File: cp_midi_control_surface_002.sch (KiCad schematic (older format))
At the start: 44 parts, among them J10 Conn_01x08_Female, J11 Conn_01x08_Female, J12 Conn_01x08_Female, J13 Conn_01x08_Female, J18 Conn_01x01_Male, J19 Conn_01x01_Male, J20 Conn_01x01_Male, J21 Conn_01x01_Male, J22 Conn_01x01_Male, J23 Conn_01x01_Male, P1 Digital, P2 Power, P3 Analogue, P4 Analogue, P5 PWM, P6 PWM, P7 Communication

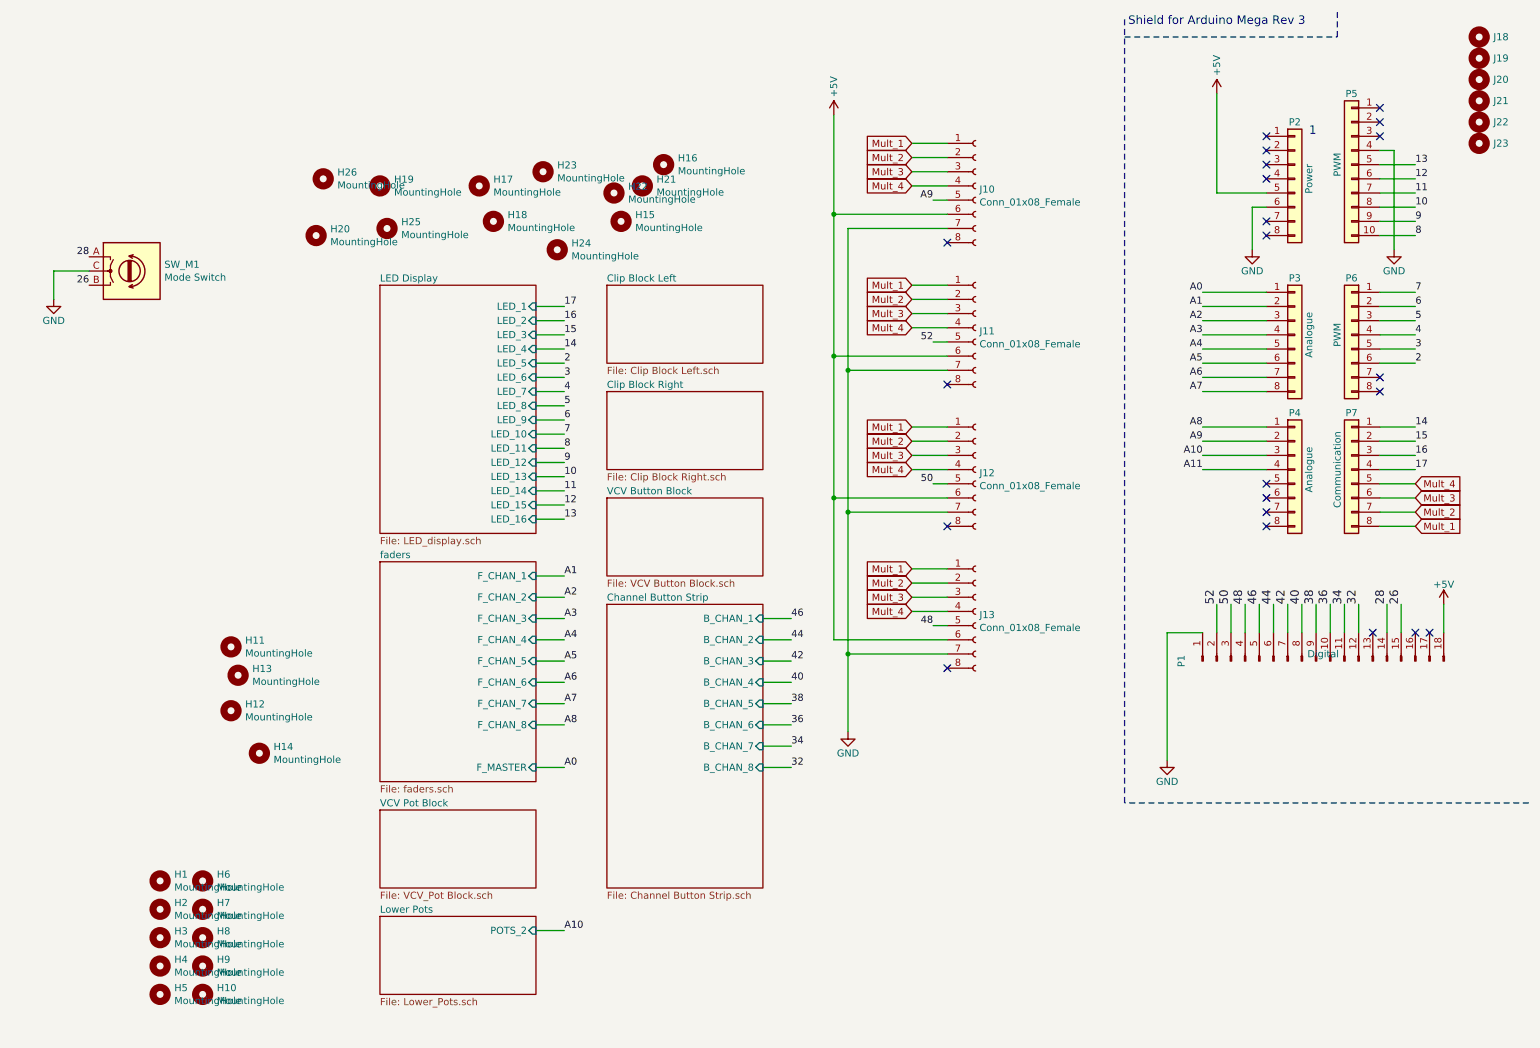
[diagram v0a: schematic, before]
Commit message: First of changes due to different software
Moving and analogue inputs, correcting for placement of multiplexer pads.
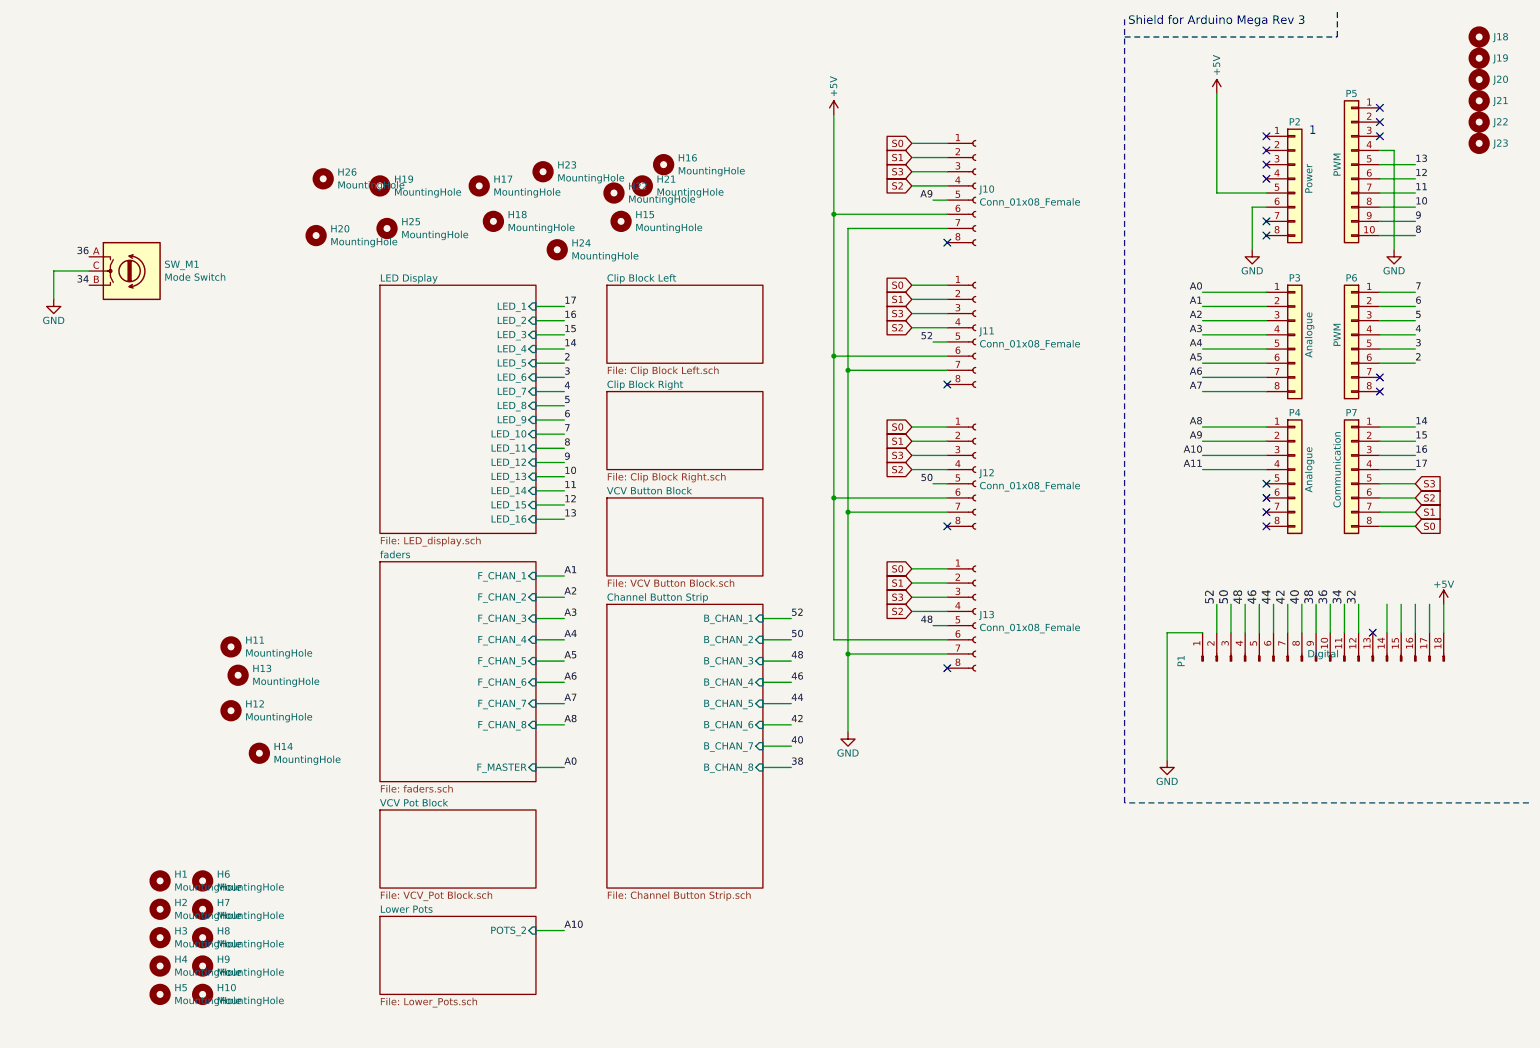
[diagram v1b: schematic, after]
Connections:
- net 34: now also SW_M1.B
- net 36: now also SW_M1.A
- net 26: no longer names the net of P1.15 (Pin_15)
- net 26: no longer SW_M1.B
- net 28: no longer names the net of P1.14 (Pin_14)
- net 28: no longer SW_M1.A
- net Mult_1 renamed S0
- net Mult_2 renamed S1
- net Mult_3 renamed S3
- net S3: now also P7.5 (Pin_5); no longer P7.6 (Pin_6)
- net Mult_4 renamed S2
- net S2: now also P7.6 (Pin_6); no longer P7.5 (Pin_5)
- no-connect marks 22 -> 20
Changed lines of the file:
@@
 Text Label 8900 3700 2    50   ~ 0
 A11
-Text Label 10300 4650 1    60   ~ 0
-26
-Text Label 10200 4650 1    60   ~ 0
-28
 Text Label 10000 4650 1    60   ~ 0
 32
@@
 $EndComp
 Text Label 1050 2200 2    50   ~ 0
-28
+36
 Text Label 1050 2400 2    50   ~ 0
-26
+34
 $Comp
 L power:GND #PWR07
@@
 A1
 Text GLabel 10400 4100 2    50   Input ~ 0
-Mult_1
+S0
 Text GLabel 10400 4000 2    50   Input ~ 0
-Mult_2
+S1
 Text GLabel 10400 3900 2    50   Input ~ 0
-Mult_3
+S2
 $Sheet
 S 3100 2400 1100 1750
@@
 	6000 5800 5800 5800
 Text Label 6000 4750 0    50   ~ 0
+52
+Text Label 6000 4900 0    50   ~ 0
+50
+Text Label 6000 5200 0    50   ~ 0
 46
-Text Label 6000 4900 0    50   ~ 0
+Text Label 6000 5050 0    50   ~ 0
+48
+Text Label 6000 5350 0    50   ~ 0
 44
-Text Label 6000 5200 0    50   ~ 0
+Text Label 6000 5500 0    50   ~ 0
+42
+Text Label 6000 5650 0    50   ~ 0
 40
-Text Label 6000 5050 0    50   ~ 0
-42
-Text Label 6000 5350 0    50   ~ 0
+Text Label 6000 5800 0    50   ~ 0
 38
-Text Label 6000 5500 0    50   ~ 0
-36
-Text Label 6000 5650 0    50   ~ 0
-34
-Text Label 6000 5800 0    50   ~ 0
-32
 Text GLabel 10400 3800 2    50   Input ~ 0
-Mult_4
+S3
 NoConn ~ 10150 3050
 NoConn ~ 10150 3150
@@
 NoConn ~ 10150 1250
 NoConn ~ 10150 1150
-NoConn ~ 10400 4850
-NoConn ~ 10500 4850
 Wire Wire Line
 	8650 4850 8650 5750
@@
 	1    0    0    -1
 $EndComp
-Text GLabel 6850 1400 0    50   Input ~ 0
-Mult_1
-Text GLabel 6850 1500 0    50   Input ~ 0
-Mult_2
-Text GLabel 6850 1600 0    50   Input ~ 0
-Mult_3
-Text GLabel 6850 1700 0    50   Input ~ 0
-Mult_4
+Text GLabel 6850 2400 0    50   Input ~ 0
+S0
+Text GLabel 6850 2500 0    50   Input ~ 0
+S1
+Text GLabel 6850 2700 0    50   Input ~ 0
+S2
+Text GLabel 6850 2600 0    50   Input ~ 0
+S3
 Wire Wire Line
 	6850 1700 7100 1700
@@
 	1    0    0    -1
 $EndComp
-Text GLabel 6850 3400 0    50   Input ~ 0
-Mult_1
-Text GLabel 6850 3500 0    50   Input ~ 0
-Mult_2
-Text GLabel 6850 3600 0    50   Input ~ 0
-Mult_3
-Text GLabel 6850 3700 0    50   Input ~ 0
-Mult_4
 Wire Wire Line
 	6850 3700 7100 3700
@@
 	1    0    0    -1
 $EndComp
-Text GLabel 6850 2400 0    50   Input ~ 0
-Mult_1
-Text GLabel 6850 2500 0    50   Input ~ 0
-Mult_2
-Text GLabel 6850 2600 0    50   Input ~ 0
-Mult_3
-Text GLabel 6850 2700 0    50   Input ~ 0
-Mult_4
 Wire Wire Line
 	6850 2700 7100 2700
@@
 	1    0    0    -1
 $EndComp
-Text GLabel 6850 4400 0    50   Input ~ 0
-Mult_1
-Text GLabel 6850 4500 0    50   Input ~ 0
-Mult_2
-Text GLabel 6850 4600 0    50   Input ~ 0
-Mult_3
-Text GLabel 6850 4700 0    50   Input ~ 0
-Mult_4
 Wire Wire Line
 	6850 4700 7100 4700
@@
 	1    0    0    -1
 $EndComp
+Text GLabel 6850 1400 0    50   Input ~ 0
+S0
+Text GLabel 6850 1500 0    50   Input ~ 0
+S1
+Text GLabel 6850 1700 0    50   Input ~ 0
+S2
+Text GLabel 6850 1600 0    50   Input ~ 0
+S3
+Text GLabel 6850 3400 0    50   Input ~ 0
+S0
+Text GLabel 6850 3500 0    50   Input ~ 0
+S1
+Text GLabel 6850 3700 0    50   Input ~ 0
+S2
+Text GLabel 6850 3600 0    50   Input ~ 0
+S3
+Text GLabel 6850 4400 0    50   Input ~ 0
+S0
+Text GLabel 6850 4500 0    50   Input ~ 0
+S1
+Text GLabel 6850 4700 0    50   Input ~ 0
+S2
+Text GLabel 6850 4600 0    50   Input ~ 0
+S3
+Wire Wire Line
+	10400 4650 10400 4850
+Wire Wire Line
+	10500 4650 10500 4850
 $EndSCHEMATC

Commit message: Sub boards completed
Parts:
- removed P4: Analogue, Socket_Arduino_Mega:Socket_Strip_Arduino_1x08, symbol Connector_Generic:Conn_01x08
- H1, H10, H11, H12, H13, H14, H15, H16, H17, H18, H19, H2, H20, H21, H22, H23, H24, H25, H26, H3, H4, H5, H6, H7, H8, H9: footprint cunabulapress-footprints:Mounting_Hole_3.2mm_M3 -> cunabulapress-footprints:Mounting_Hole_M3_with_Target
- P2, P3, P6: footprint Socket_Arduino_Mega:Socket_Strip_Arduino_1x08 -> Connector_PinHeader_2.54mm:PinHeader_1x08_P2.54mm_Vertical
- P5: footprint Socket_Arduino_Mega:Socket_Strip_Arduino_1x10 -> Connector_PinHeader_2.54mm:PinHeader_1x10_P2.54mm_Vertical
- P7: footprint Socket_Arduino_Mega:Socket_Strip_Arduino_1x08 -> Connector_PinHeader_2.54mm:PinHeader_1x04_P2.54mm_Vertical; symbol Connector_Generic:Conn_01x08 -> Connector_Generic:Conn_01x04
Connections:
- net A9 is gone; now on net A0: J10.5 (Pin_5)
- net A1: now also J11.5 (Pin_5)
- net A2: now also J12.5 (Pin_5)
- net A3: now also J13.5 (Pin_5)
- net S0: now also P1.17 (Pin_17); no longer P7.8 (Pin_8)
- net S1: now also P1.16 (Pin_16); no longer P7.7 (Pin_7)
- net S2: now also P1.14 (Pin_14); no longer P7.6 (Pin_6)
- net S3: now also P1.15 (Pin_15); no longer P7.5 (Pin_5)
- net 32 renamed 33
- net 34 renamed 35
- net 36 renamed 37
- net 38 renamed 39
- net 40 renamed 41
- net 42 renamed 43
- net 44 renamed 45
- net 46 renamed 47
- net 48 renamed 49
- net 49: no longer J13.5 (Pin_5)
- net 50 renamed 51
- net 51: no longer J12.5 (Pin_5)
- net 52 renamed 53
- net 53: no longer J11.5 (Pin_5)
- net A6: no longer names the net of P3.7 (Pin_7)
- net A7: no longer names the net of P3.8 (Pin_8)
- no-connect marks 20 -> 18

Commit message: Tidy schematic / renumber components / complete daughter boards
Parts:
- removed J18, J19, J20, J21, J22, J23: Conn_01x01_Male, cunabulapress-footprints:Arduino_1pin_EDIT, symbol Mechanical:MountingHole
- H1, H26: value MountingHole -> ~
- H10: renamed from H23; value MountingHole -> ~
- H11: renamed from H6; value MountingHole -> ~
- H12: renamed from H8; value MountingHole -> ~
- H13: renamed from H19; value MountingHole -> ~
- H14: renamed from H24; value MountingHole -> ~
- H15: renamed from H9; value MountingHole -> ~
- H16: renamed from H10; value MountingHole -> ~
- H17: renamed from H11; value MountingHole -> ~
- H18: renamed from H12; value MountingHole -> ~
- H19: renamed from H20; value MountingHole -> ~
- H2: renamed from H3; value MountingHole -> ~
- H20: renamed from H25; value MountingHole -> ~
- H21: renamed from H13; value MountingHole -> ~
- H22: renamed from H15; value MountingHole -> ~
- H23: renamed from H14; value MountingHole -> ~
- H24: renamed from H16; value MountingHole -> ~
- H25: renamed from H21; value MountingHole -> ~
- H3: renamed from H17; value MountingHole -> ~
- H4: renamed from H22; value MountingHole -> ~
- H5: renamed from H2; value MountingHole -> ~
- H6: renamed from H4; value MountingHole -> ~
- H7: renamed from H5; value MountingHole -> ~
- H8: renamed from H7; value MountingHole -> ~
- H9: renamed from H18; value MountingHole -> ~
- J2: renamed from J10; value Conn_01x08_Female -> ~; symbol Connector:Conn_01x08_Female -> Connector:Conn_01x08_Male
- J4: renamed from J11; value Conn_01x08_Female -> ~; symbol Connector:Conn_01x08_Female -> Connector:Conn_01x08_Male
- J6: renamed from J12; value Conn_01x08_Female -> ~; symbol Connector:Conn_01x08_Female -> Connector:Conn_01x08_Male
- J8: renamed from J13; value Conn_01x08_Female -> ~; symbol Connector:Conn_01x08_Female -> Connector:Conn_01x08_Male
- P3: renamed from P1; footprint Connector_PinSocket_2.54mm:PinSocket_1x18_P2.54mm_Vertical -> Connector_PinHeader_2.54mm:PinHeader_1x18_P2.54mm_Vertical; symbol Connector:Conn_01x18_Male -> Connector_Generic:Conn_01x18
- SW_M1: value Mode Switch -> EC12E
- renumbered P2 to P1, P3 to P2, P7 to P4, P6 to P5, P5 to P6
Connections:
- net 33: no longer names the net of P3.12 (Pin_12)
- no-connect marks 18 -> 19
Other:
- note added: "Arduino Mega Rev 3"
- note added: "Connections on main board"
- note added: "Daughter boards connected by pin header"
- note added: "Daughter boards connected by ribbon cable"
- note added: "Main Board"
- note added: "Mounting holes (M3)"
- note removed: "Shield for Arduino Mega Rev 3"
- moved on the sheet: H1, H10, H11, H12, H13, H14, H15, H16, H17, H18, H19, H2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

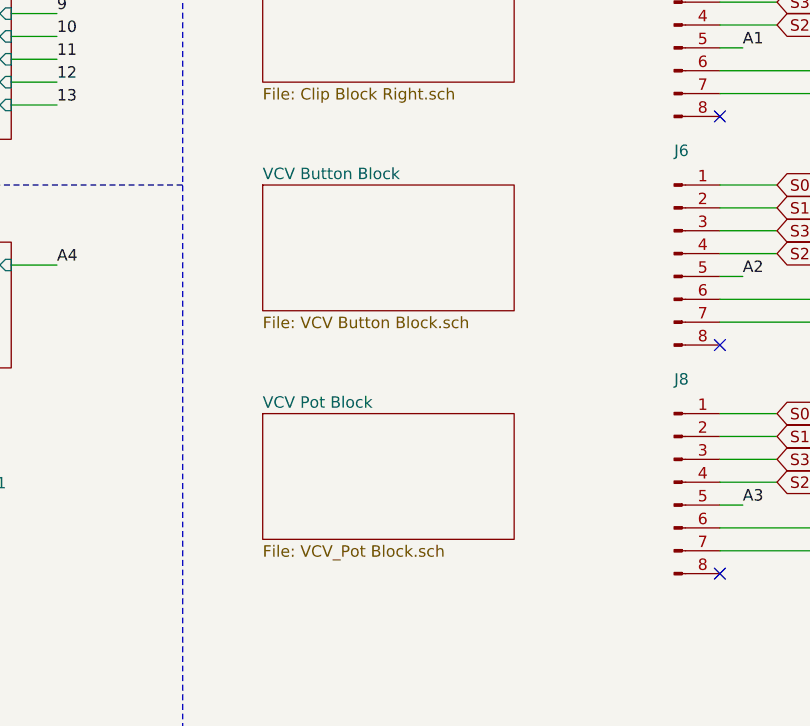
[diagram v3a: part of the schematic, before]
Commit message: Redesign of upper boards
Added bussed resistors following Igor's correction to the schematic + tidied schematic.
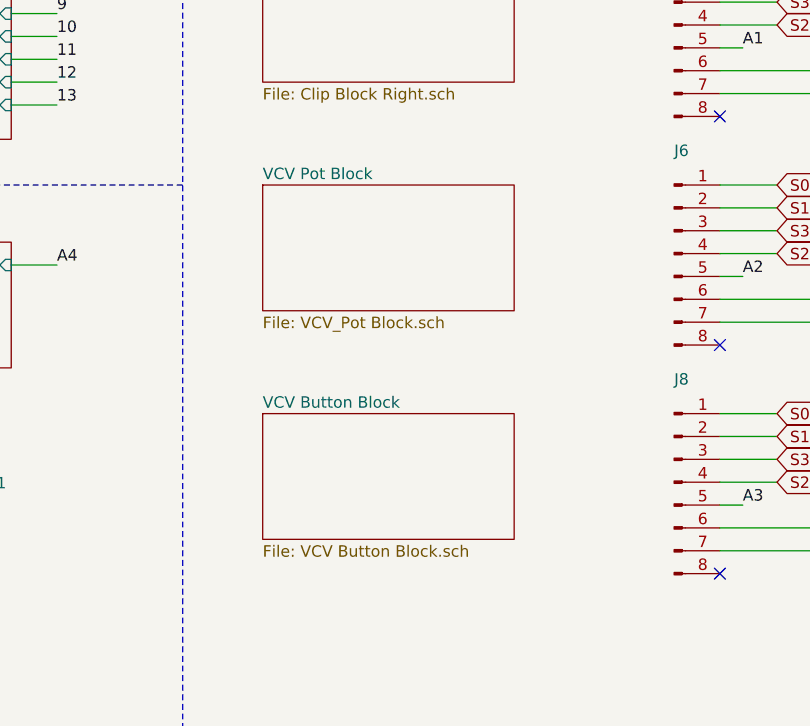
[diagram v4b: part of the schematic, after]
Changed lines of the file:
@@
 	3750 1400 3950 1400
 $Sheet
-S 4850 4250 1100 550
+S 4850 3250 1100 550
 U 5C3B66BD
 F0 "VCV Pot Block" 50
@@
 $EndSheet
 $Sheet
-S 4850 3250 1100 550
+S 4850 4250 1100 550
 U 5C4BAA18
 F0 "VCV Button Block" 50
